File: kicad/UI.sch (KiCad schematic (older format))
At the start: 12 parts, among them Q14 DMN3065LW-7, SW2 UPLOAD, U8 PCA9632

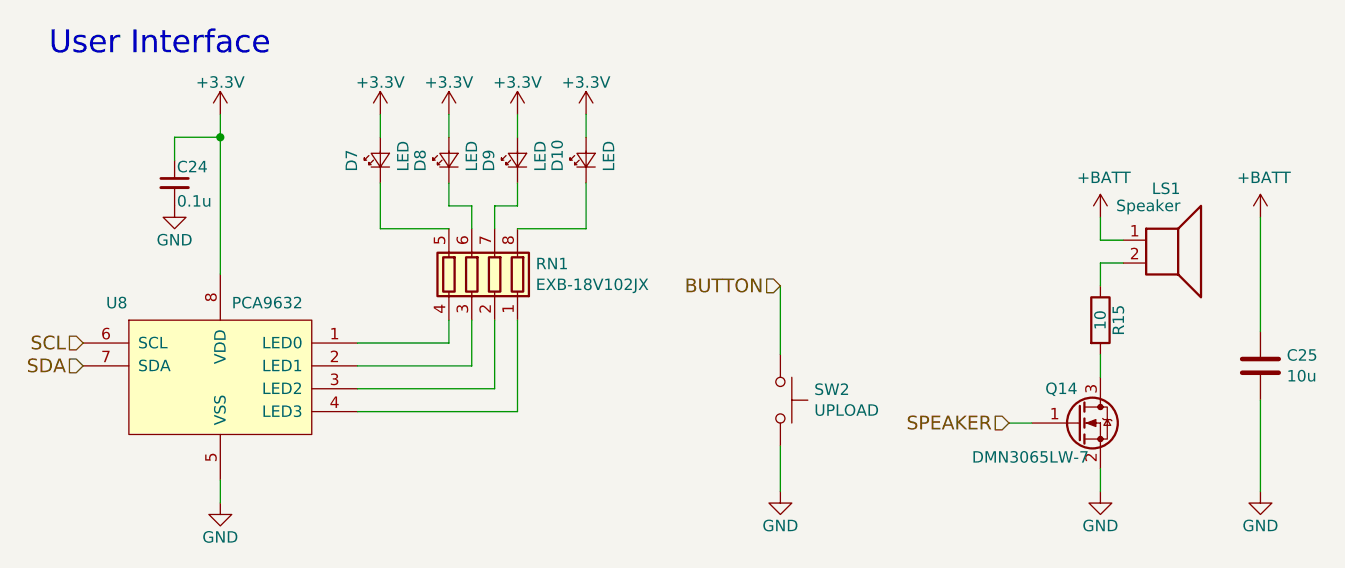
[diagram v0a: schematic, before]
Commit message: 部品を配置
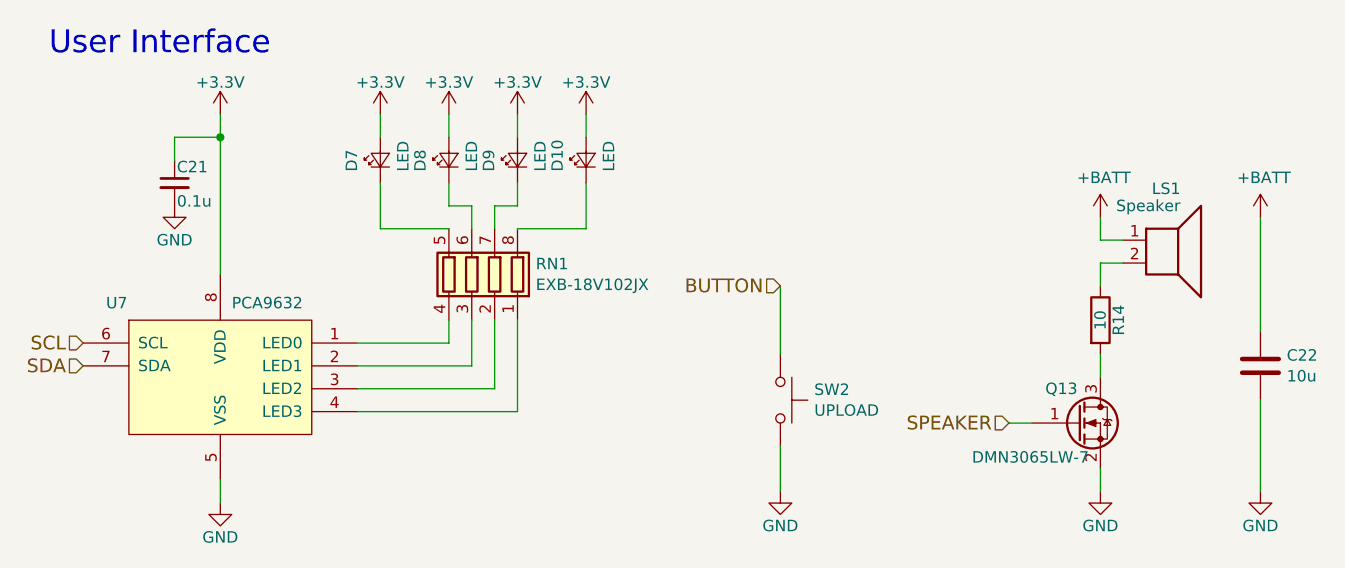
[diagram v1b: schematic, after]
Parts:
- renumbered C24 to C21, C25 to C22, Q14 to Q13, R15 to R14, U8 to U7
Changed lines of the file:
@@
 EESchema Schematic File Version 4
 LIBS:KERISE-cache
-EELAYER 26 0
+EELAYER 29 0
 EELAYER END
 $Descr A4 11693 8268
 encoding utf-8
-Sheet 14 15
+Sheet 14 13
 Title ""
 Date ""
@@
 $EndDescr
 $Comp
-L power:GND #PWR078
+L power:GND #PWR068
 U 1 1 57CEA2EF
 P 6500 4600
-F 0 "#PWR078" H 6500 4350 50  0001 C CNN
+F 0 "#PWR068" H 6500 4350 50  0001 C CNN
 F 1 "GND" H 6500 4450 50  0000 C CNN
 F 2 "" H 6500 4600 50  0000 C CNN
@@
 	6500 4600 6500 4400
 $Comp
-L power:GND #PWR080
+L power:GND #PWR070
 U 1 1 5A1C53C4
 P 7900 4600
-F 0 "#PWR080" H 7900 4350 50  0001 C CNN
+F 0 "#PWR070" H 7900 4350 50  0001 C CNN
 F 1 "GND" H 7900 4450 50  0000 C CNN
 F 2 "" H 7900 4600 50  0000 C CNN
@@
 SDA
 $Comp
-L power:+3.3V #PWR072
+L power:+3.3V #PWR062
 U 1 1 5A202D5A
 P 4050 2950
-F 0 "#PWR072" H 4050 2800 50  0001 C CNN
+F 0 "#PWR062" H 4050 2800 50  0001 C CNN
 F 1 "+3.3V" H 4050 3090 50  0000 C CNN
 F 2 "" H 4050 2950 50  0001 C CNN
@@
 	4050 2950 4050 3050
 $Comp
-L power:GND #PWR073
+L power:GND #PWR063
 U 1 1 5A202F53
 P 4050 4650
-F 0 "#PWR073" H 4050 4400 50  0001 C CNN
+F 0 "#PWR063" H 4050 4400 50  0001 C CNN
 F 1 "GND" H 4050 4500 50  0000 C CNN
 F 2 "" H 4050 4650 50  0000 C CNN
@@
 	5050 3050 5050 2950
 $Comp
-L power:+3.3V #PWR075
+L power:+3.3V #PWR065
 U 1 1 5A204571
 P 5050 2950
-F 0 "#PWR075" H 5050 2800 50  0001 C CNN
+F 0 "#PWR065" H 5050 2800 50  0001 C CNN
 F 1 "+3.3V" H 5050 3090 50  0000 C CNN
 F 2 "" H 5050 2950 50  0001 C CNN
@@
 	4750 3050 4750 2950
 $Comp
-L power:+3.3V #PWR074
+L power:+3.3V #PWR064
 U 1 1 5A203D72
 P 4750 2950
-F 0 "#PWR074" H 4750 2800 50  0001 C CNN
+F 0 "#PWR064" H 4750 2800 50  0001 C CNN
 F 1 "+3.3V" H 4750 3090 50  0000 C CNN
 F 2 "" H 4750 2950 50  0001 C CNN
@@
 	5650 3050 5650 2950
 $Comp
-L power:+3.3V #PWR077
+L power:+3.3V #PWR067
 U 1 1 5A20460C
 P 5650 2950
-F 0 "#PWR077" H 5650 2800 50  0001 C CNN
+F 0 "#PWR067" H 5650 2800 50  0001 C CNN
 F 1 "+3.3V" H 5650 3090 50  0000 C CNN
 F 2 "" H 5650 2950 50  0001 C CNN
@@
 	5350 3050 5350 2950
 $Comp
-L power:+3.3V #PWR076
+L power:+3.3V #PWR066
 U 1 1 5A204620
 P 5350 2950
-F 0 "#PWR076" H 5350 2800 50  0001 C CNN
+F 0 "#PWR066" H 5350 2800 50  0001 C CNN
 F 1 "+3.3V" H 5350 3090 50  0000 C CNN
 F 2 "" H 5350 2950 50  0001 C CNN
@@
 $EndComp
 $Comp
-L Device:C_Small C24
+L Device:C_Small C21
 U 1 1 5A2A1F42
 P 3850 3250
-F 0 "C24" H 3860 3320 50  0000 L CNN
+F 0 "C21" H 3860 3320 50  0000 L CNN
 F 1 "0.1u" H 3860 3170 50  0000 L CNN
 F 2 "Capacitor_SMD:C_0201_0603Metric" H 3850 3250 50  0001 C CNN
@@
 $EndComp
 $Comp
-L power:GND #PWR071
+L power:GND #PWR061
 U 1 1 5A2A2041
 P 3850 3350
-F 0 "#PWR071" H 3850 3100 50  0001 C CNN
+F 0 "#PWR061" H 3850 3100 50  0001 C CNN
 F 1 "GND" H 3850 3200 50  0000 C CNN
 F 2 "" H 3850 3350 50  0001 C CNN
@@
 Connection ~ 4050 3050
 $Comp
-L KERISE:PCA9632 U8
+L KERISE:PCA9632 U7
 U 1 1 5A2BFCCE
 P 4050 4100
-F 0 "U8" H 3550 4425 50  0000 L CNN
+F 0 "U7" H 3550 4425 50  0000 L CNN
 F 1 "PCA9632" H 4100 4425 50  0000 L CNN
 F 2 "mouse:DFN-8-1EP_3x3mm_Pitch0.5mm" H 4100 3800 50  0001 L CNN
@@
 $EndComp
 $Comp
-L Device:Q_NMOS_GSD Q14
+L Device:Q_NMOS_GSD Q13
 U 1 1 5B6723D7
 P 7800 4300
-F 0 "Q14" H 7800 4450 50  0000 R CNN
+F 0 "Q13" H 7800 4450 50  0000 R CNN
 F 1 "DMN3065LW-7" H 7850 4150 50  0000 R CNN
 F 2 "Package_TO_SOT_SMD:SOT-323_SC-70" H 8000 4400 50  0001 C CNN
@@
 	7500 4300 7600 4300
 $Comp
-L Device:R R15
+L Device:R R14
 U 1 1 5B6725CD
 P 7900 3850
-F 0 "R15" V 7980 3850 50  0000 C CNN
+F 0 "R14" V 7980 3850 50  0000 C CNN
 F 1 "10" V 7900 3850 50  0000 C CNN
 F 2 "Resistor_SMD:R_0201_0603Metric" V 7830 3850 50  0001 C CNN
@@
 $EndComp
 $Comp
-L power:+BATT #PWR079
+L power:+BATT #PWR069
 U 1 1 5C29DB6A
 P 7900 3400
-F 0 "#PWR079" H 7900 3250 50  0001 C CNN
+F 0 "#PWR069" H 7900 3250 50  0001 C CNN
 F 1 "+BATT" H 7915 3573 50  0000 C CNN
 F 2 "" H 7900 3400 50  0001 C CNN
@@
 $EndComp
 $Comp
-L Device:C C25
+L Device:C C22
 U 1 1 5C29E0A6
 P 8600 4050
-F 0 "C25" H 8715 4096 50  0000 L CNN
+F 0 "C22" H 8715 4096 50  0000 L CNN
 F 1 "10u" H 8715 4005 50  0000 L CNN
 F 2 "Capacitor_SMD:C_0402_1005Metric" H 8638 3900 50  0001 C CNN
@@
 $EndComp
 $Comp
-L power:+BATT #PWR081
+L power:+BATT #PWR071
 U 1 1 5C29E17B
 P 8600 3400
-F 0 "#PWR081" H 8600 3250 50  0001 C CNN
+F 0 "#PWR071" H 8600 3250 50  0001 C CNN
 F 1 "+BATT" H 8615 3573 50  0000 C CNN
 F 2 "" H 8600 3400 50  0001 C CNN
@@
 $EndComp
 $Comp
-L power:GND #PWR082
+L power:GND #PWR072
 U 1 1 5C29E1A4
 P 8600 4600
-F 0 "#PWR082" H 8600 4350 50  0001 C CNN
+F 0 "#PWR072" H 8600 4350 50  0001 C CNN
 F 1 "GND" H 8600 4450 50  0000 C CNN
 F 2 "" H 8600 4600 50  0000 C CNN
